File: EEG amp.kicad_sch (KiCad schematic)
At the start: 38 parts, among them J1 Electrodes, J2 Power, J3 Output, J4 Status, U1 AD8232, U2 TMUX154EDGS

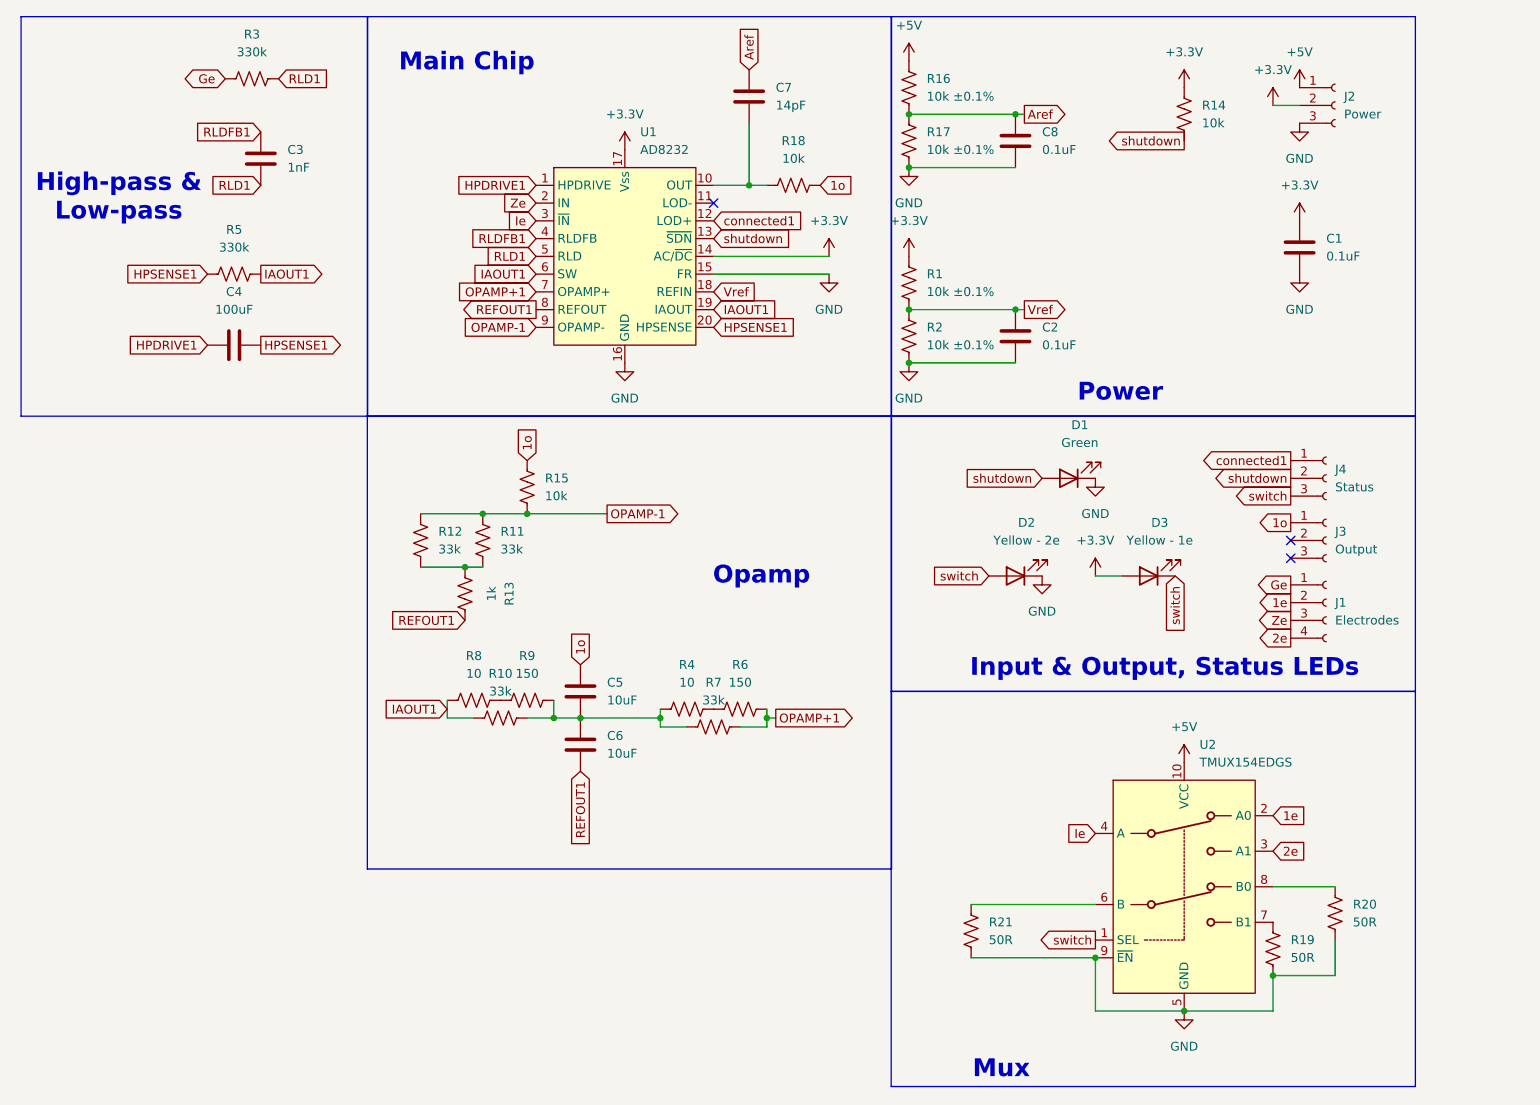
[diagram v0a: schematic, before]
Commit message: Organized better and got some tips from from a professional PCB designer :3
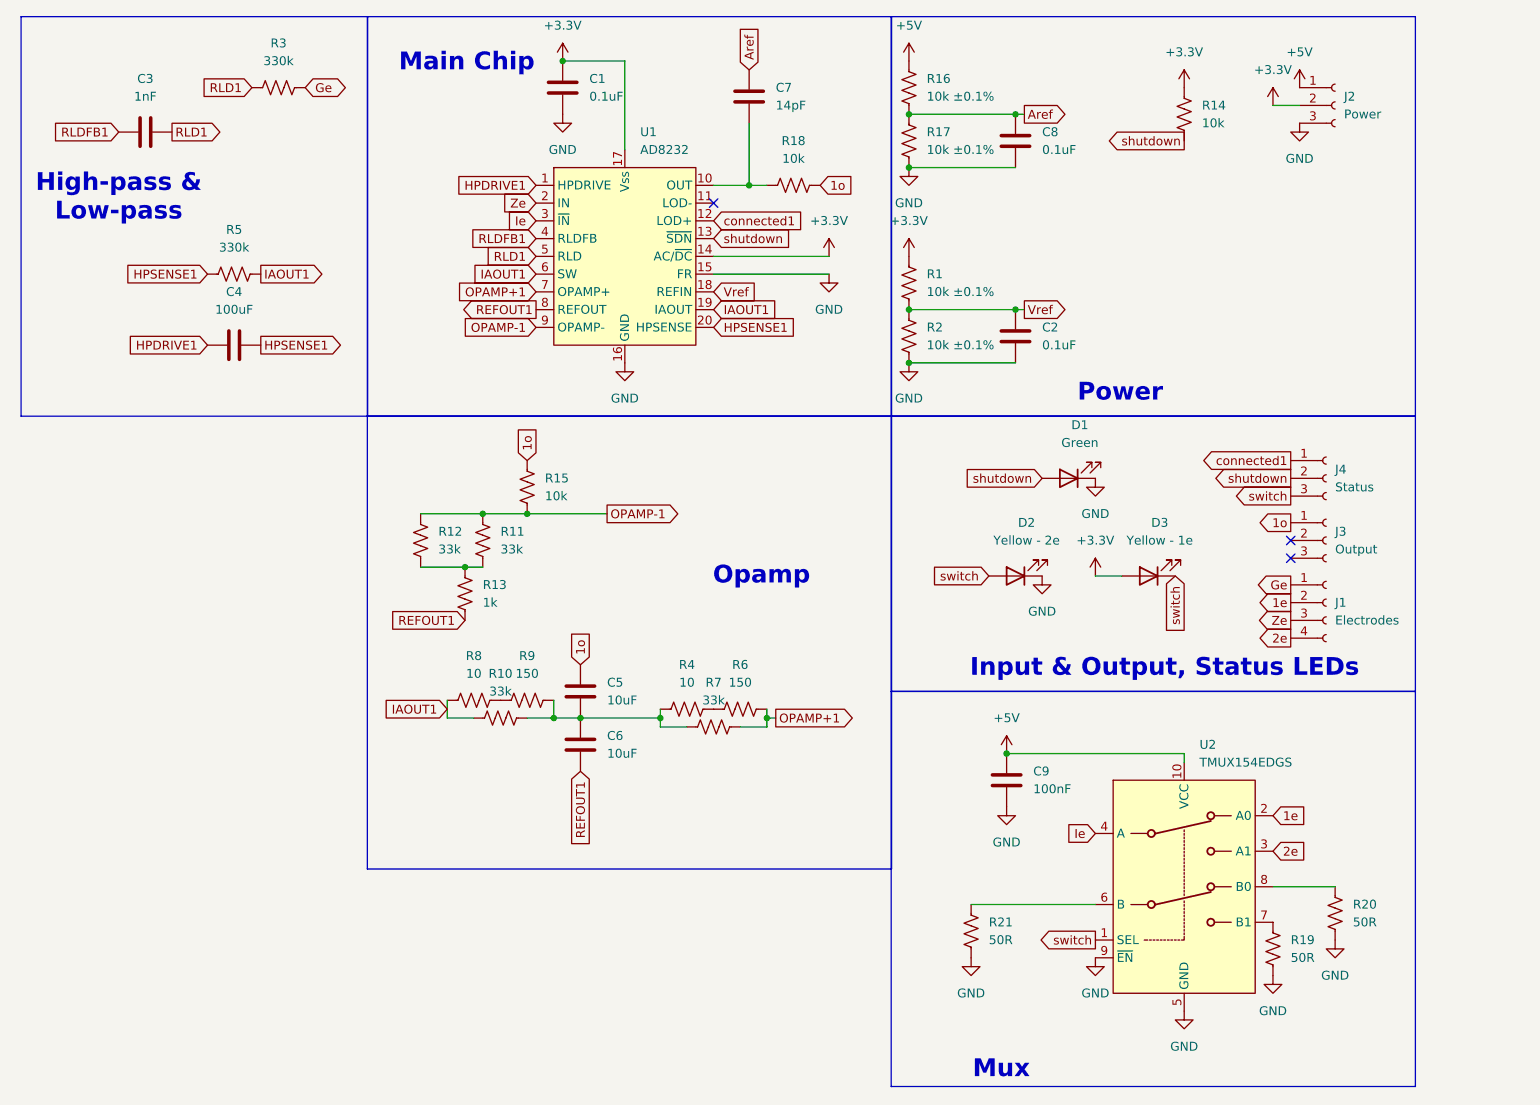
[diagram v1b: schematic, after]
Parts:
- added C9: 100nF, Capacitor_SMD:C_0201_0603Metric, symbol Device:C
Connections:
- net +5V: now also C9.1
- net GND: now also C9.2
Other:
- moved on the sheet: C1, C3, R3

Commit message: Designed PCB and apparently did something to the schematic
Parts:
- added D4: Red, LED_THT:LED_D5.0mm, symbol Device:LED
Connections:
- net +3.3V: now also D4.2 (A)
- net connected1: now also D4.1 (K)
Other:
- moved on the sheet: D1, D3
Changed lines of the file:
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@@
 	(wire
 		(pts
-			(xy 238.76 92.71) (xy 242.57 92.71)
+			(xy 234.95 95.25) (xy 238.76 95.25)
 		)
 		(stroke
@@
 	(global_label "connected1"
 		(shape input)
+		(at 251.46 80.01 270)
+		(fields_autoplaced yes)
+		(effects
+			(font
+				(size 1.27 1.27)
+			)
+			(justify right)
+		)
+		(property "Intersheetrefs" "${INTERSHEET_REFS}"
+			(at 251.46 93.8808 90)
+			(effects
+				(font
+					(size 1.27 1.27)
+				)
+				(justify right)
+				(hide yes)
+			)
+		)
+	)
+	(global_label "connected1"
+		(shape input)
 		(at 184.15 41.91 0)
 		(fields_autoplaced yes)
@@
 	(global_label "switch"
 		(shape input)
-		(at 250.19 92.71 270)
+		(at 246.38 95.25 270)
 		(fields_autoplaced yes)
 		(effects
@@
 		)
 		(property "Intersheetrefs" "${INTERSHEET_REFS}"
-			(at 250.19 101.6219 90)
+			(at 246.38 104.1619 90)
 			(effects
 				(font
@@
 	(global_label "shutdown"
 		(shape input)
-		(at 231.14 78.74 180)
+		(at 226.06 78.74 180)
 		(fields_autoplaced yes)
 		(effects
@@
 		)
 		(property "Intersheetrefs" "${INTERSHEET_REFS}"
-			(at 219.3255 78.74 0)
+			(at 214.2455 78.74 0)
 			(effects
 				(font
@@
 	)
 	(symbol
+		(lib_id "Device:LED")
+		(at 247.65 80.01 180)
+		(unit 1)
+		(exclude_from_sim no)
+		(in_bom yes)
+		(on_board yes)
+		(dnp no)
+		(fields_autoplaced yes)
+		(property "Reference" "D4"
+			(at 249.2375 72.39 0)
+			(effects
+				(font
+					(size 1.27 1.27)
+				)
+			)
+		)
+		(property "Value" "Red"
+			(at 249.2375 74.93 0)
+			(effects
+				(font
+					(size 1.27 1.27)
+				)
+			)
+		)
+		(property "Footprint" "LED_THT:LED_D5.0mm"
+			(at 247.65 80.01 0)
+			(effects
+				(font
+					(size 1.27 1.27)
+				)
+				(hide yes)
+			)
+		)
+		(property "Datasheet" "~"
+			(at 247.65 80.01 0)
+			(effects
+				(font
+					(size 1.27 1.27)
+				)
+				(hide yes)
+			)
+		)
+		(property "Description" "Light emitting diode"
+			(at 247.65 80.01 0)
+			(effects
+				(font
+					(size 1.27 1.27)
+				)
+				(hide yes)
+			)
+		)
+		(pin "2"
+		)
+		(pin "1"
+		)
+		(instances
+			(project "EEG amp"
+				(path "/828fcb53-5b19-4d8c-be04-4f1b7f282370"
+					(reference "D4")
+					(unit 1)
+				)
+			)
+		)
+	)
+	(symbol
 		(lib_id "power:GND")
 		(at 200.66 49.53 0)
@@
 	(symbol
 		(lib_id "Device:LED")
-		(at 246.38 92.71 180)
+		(at 242.57 95.25 180)
 		(unit 1)
 		(exclude_from_sim no)
@@
 		(fields_autoplaced yes)
 		(property "Reference" "D3"
-			(at 247.9675 85.09 0)
+			(at 244.1575 87.63 0)
 			(effects
 				(font
@@
 		)
 		(property "Value" "Yellow - 1e"
-			(at 247.9675 87.63 0)
+			(at 244.1575 90.17 0)
 			(effects
 				(font
@@
 		)
 		(property "Footprint" "LED_THT:LED_D5.0mm"
-			(at 246.38 92.71 0)
+			(at 242.57 95.25 0)
 			(effects
 				(font
@@
 		)
 		(property "Datasheet" "~"
-			(at 246.38 92.71 0)
+			(at 242.57 95.25 0)
 			(effects
 				(font
@@
 		)
 		(property "Description" "Light emitting diode"
-			(at 246.38 92.71 0)
+			(at 242.57 95.25 0)
 			(effects
 				(font
@@
 	)
 	(symbol
+		(lib_id "power:+3.3V")
+		(at 243.84 80.01 0)
+		(unit 1)
+		(exclude_from_sim no)
+		(in_bom yes)
+		(on_board yes)
+		(dnp no)
+		(fields_autoplaced yes)
+		(property "Reference" "#PWR024"
+			(at 243.84 83.82 0)
+			(effects
+				(font
+					(size 1.27 1.27)
+				)
+				(hide yes)
+			)
+		)
+		(property "Value" "+3.3V"
+			(at 243.84 74.93 0)
+			(effects
+				(font
+					(size 1.27 1.27)
+				)
+			)
+		)
+		(property "Footprint" ""
+			(at 243.84 80.01 0)
+			(effects
+				(font
+					(size 1.27 1.27)
+				)
+				(hide yes)
+			)
+		)
+		(property "Datasheet" ""
+			(at 243.84 80.01 0)
+			(effects
+				(font
+					(size 1.27 1.27)
+				)
+				(hide yes)
+			)
+		)
+		(property "Description" "Power symbol creates a global label with name \"+3.3V\""
+			(at 243.84 80.01 0)
+			(effects
+				(font
+					(size 1.27 1.27)
+				)
+				(hide yes)
+			)
+		)
+		(pin "1"
+		)
+		(instances
+			(project "EEG amp"
+				(path "/828fcb53-5b19-4d8c-be04-4f1b7f282370"
+					(reference "#PWR024")
+					(unit 1)
+				)
+			)
+		)
+	)
+	(symbol
 		(lib_id "Device:C")
 		(at 165.1 109.22 180)
@@
 	(symbol
 		(lib_id "power:+3.3V")
-		(at 238.76 92.71 0)
+		(at 234.95 95.25 0)
 		(unit 1)
 		(exclude_from_sim no)
@@
 		(fields_autoplaced yes)
 		(property "Reference" "#PWR019"
-			(at 238.76 96.52 0)
+			(at 234.95 99.06 0)
 			(effects
 				(font
@@
 		)
 		(property "Value" "+3.3V"
-			(at 238.76 87.63 0)
+			(at 234.95 90.17 0)
 			(effects
 				(font
@@
 		)
 		(property "Footprint" ""
-			(at 238.76 92.71 0)
+			(at 234.95 95.25 0)
 			(effects
 				(font
@@
 		)
 		(property "Datasheet" ""
-			(at 238.76 92.71 0)
+			(at 234.95 95.25 0)
 			(effects
 				(font
@@
 		)
 		(property "Description" "Power symbol creates a global label with name \"+3.3V\""
-			(at 238.76 92.71 0)
+			(at 234.95 95.25 0)
 			(effects
 				(font
@@
 	(symbol
 		(lib_id "Device:LED")
-		(at 234.95 78.74 180)
+		(at 229.87 78.74 180)
 		(unit 1)
 		(exclude_from_sim no)
@@
 		(fields_autoplaced yes)
 		(property "Reference" "D1"
-			(at 236.5375 71.12 0)
+			(at 231.4575 71.12 0)
 			(effects
 				(font
@@
 		)
 		(property "Value" "Green"
-			(at 236.5375 73.66 0)
+			(at 231.4575 73.66 0)
 			(effects
 				(font
@@
 		)
 		(property "Footprint" "LED_THT:LED_D5.0mm"
-			(at 234.95 78.74 0)
+			(at 229.87 78.74 0)
 			(effects
 				(font
@@
 		)
 		(property "Datasheet" "~"
-			(at 234.95 78.74 0)
+			(at 229.87 78.74 0)
 			(effects
 				(font
@@
 		)
 		(property "Description" "Light emitting diode"
-			(at 234.95 78.74 0)
+			(at 229.87 78.74 0)
 			(effects
 				(font
@@
 	(symbol
 		(lib_id "power:GND")
-		(at 238.76 78.74 0)
+		(at 233.68 78.74 0)
 		(unit 1)
 		(exclude_from_sim no)
@@
 		(fields_autoplaced yes)
 		(property "Reference" "#PWR016"
-			(at 238.76 85.09 0)
+			(at 233.68 85.09 0)
 			(effects
 				(font
@@
 		)
 		(property "Value" "GND"
-			(at 238.76 83.82 0)
+			(at 233.68 83.82 0)
 			(effects
 				(font
@@
 		)
 		(property "Footprint" ""
-			(at 238.76 78.74 0)
+			(at 233.68 78.74 0)
 			(effects
 				(font
@@
 		)
 		(property "Datasheet" ""
-			(at 238.76 78.74 0)
+			(at 233.68 78.74 0)
 			(effects
 				(font
@@
 		)
 		(property "Description" "Power symbol creates a global label with name \"GND\" , ground"
-			(at 238.76 78.74 0)
+			(at 233.68 78.74 0)
 			(effects
 				(font

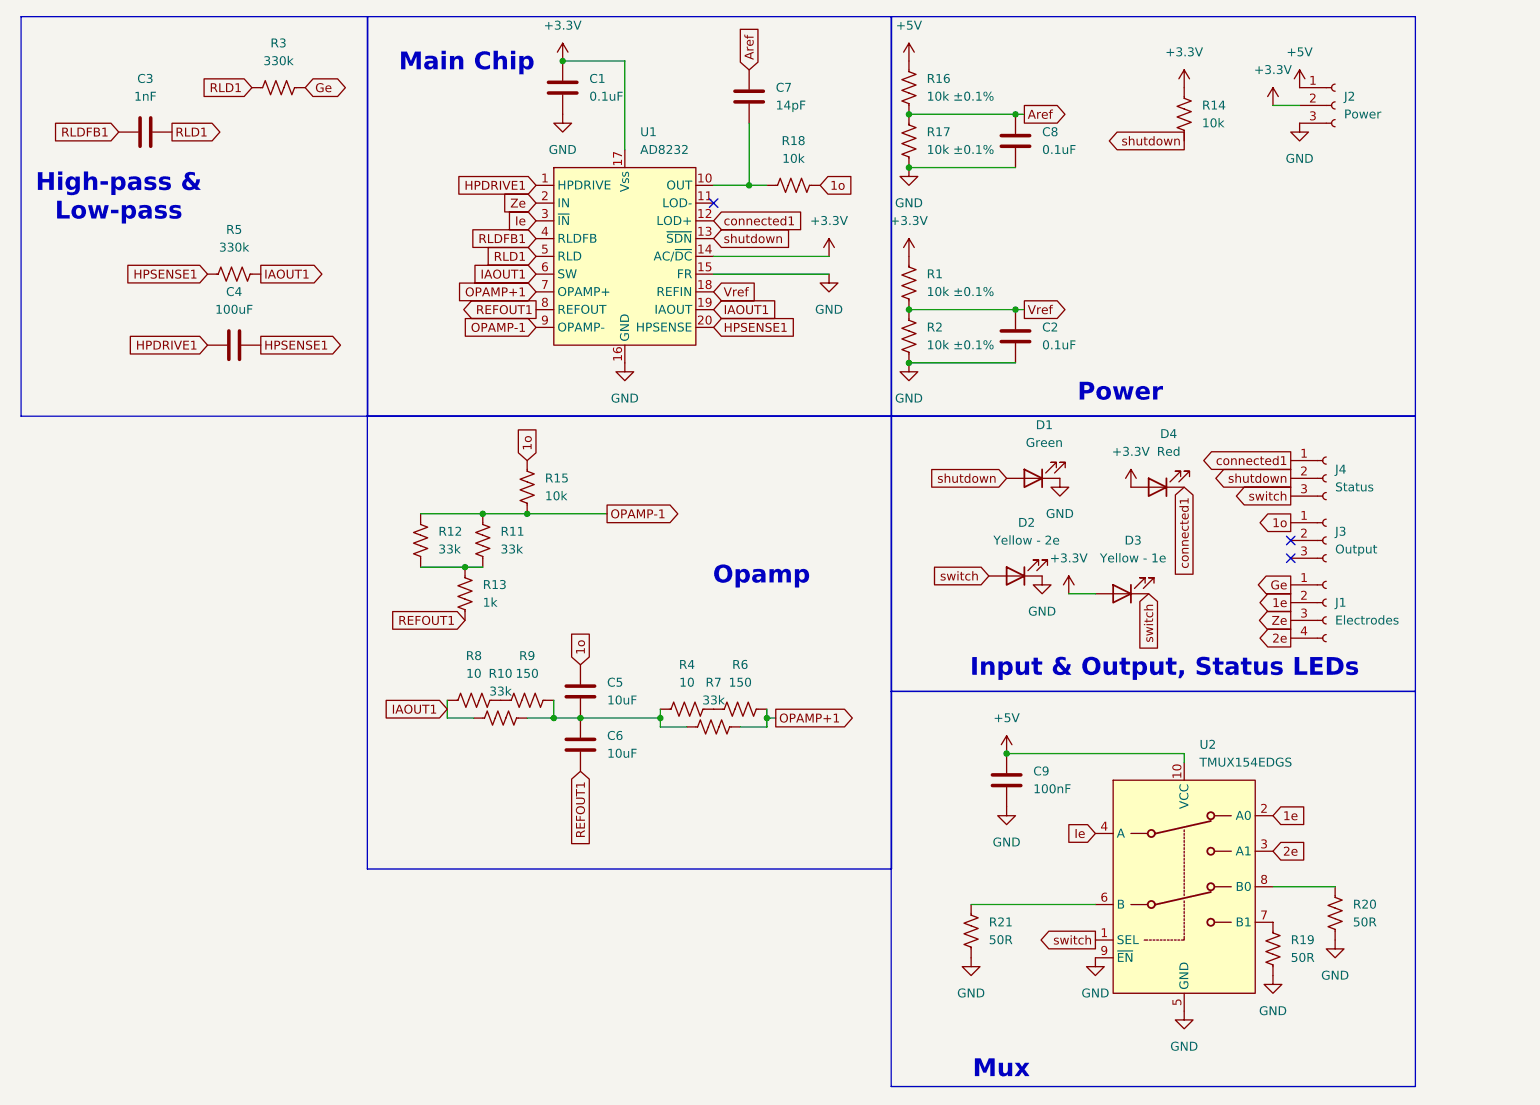
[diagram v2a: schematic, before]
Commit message: Changed gitignore, reorganized schematic a bit, connected EP to ground, and updated the symbol
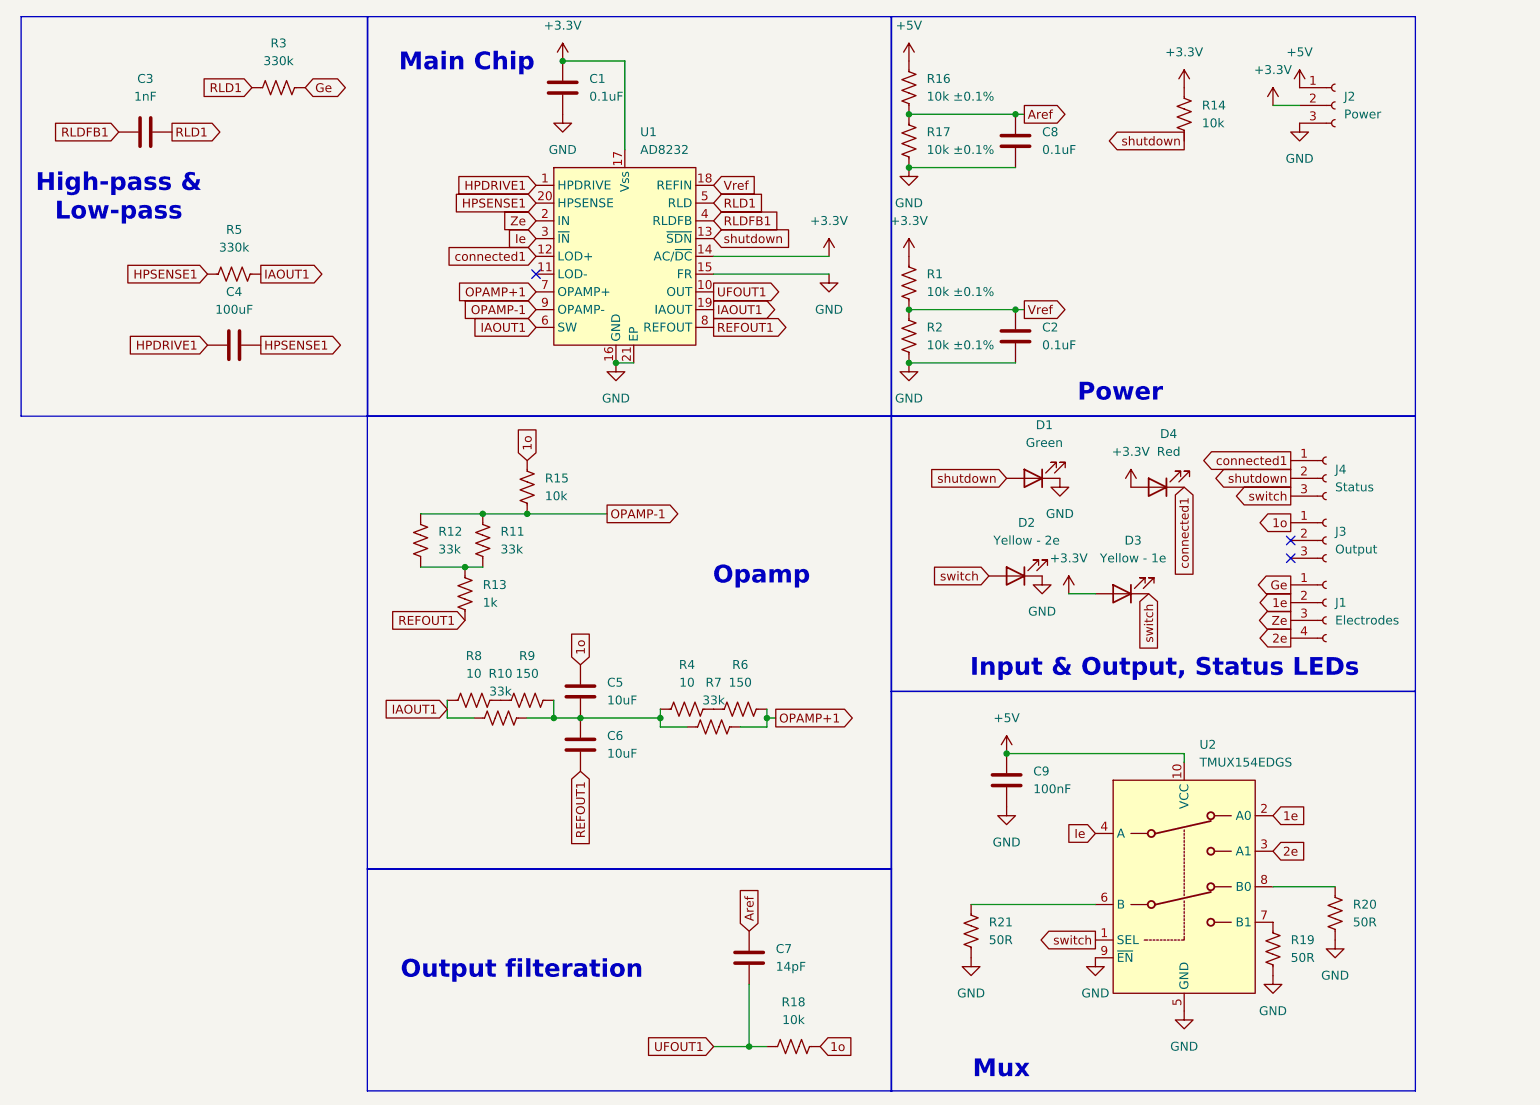
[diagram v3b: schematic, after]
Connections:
- net GND: now also U1.21 (EP)
- net UFOUT1: now reaches C7.2, R18.1, U1.10 (OUT)
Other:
- note added: "Output filteration"
- moved on the sheet: C7
